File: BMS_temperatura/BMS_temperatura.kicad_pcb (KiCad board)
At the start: 2 copper layers, 100.1 x 100.1 mm, 148 parts, among them J101 Conn_01x08_Male, Q101 MMBT3904, U1 UFRGS_PILL, U101 74HC4051, U103 74HC4051, U105 74HC4051, U112 LM324, U1801 LM324, U1901 LM324, U2001 LM324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

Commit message: layout att 3
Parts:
- TP22: value VCC -> GND
- moved R105 166.8 mm to (98.4, 183.8), turned to 90 degrees
- moved R101 162.1 mm to (81.5, 183.8), turned to 90 degrees
- moved R107 158.7 mm to (116.0, 183.8), turned to 90 degrees
- moved TP27 119.0 mm to (166.7, 163.2)
- moved C106 110.9 mm to (61.3, 153.3)
- moved F301 92.4 mm to (161.5, 101.4), turned to 270 degrees
- moved C103 92.0 mm to (61.3, 151.0)
- moved C101 89.3 mm to (61.3, 148.9)
- moved FB301 84.3 mm to (161.5, 97.0), turned to 270 degrees
- moved TP20 79.9 mm to (110.6, 138.9)
- moved D302 79.8 mm to (83.2, 24.1)
- moved TP18 79.8 mm to (115.5, 135.8)
- moved D301 79.7 mm to (166.5, 100.8), turned to 90 degrees
- moved TP21 74.2 mm to (182.6, 99.9)
- moved TP22 73.4 mm to (163.5, 112.3)
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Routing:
- net GND: track 138.2 -> 290.7 mm, vias 0 -> 2
- net /S2: track 45.3 -> 124.0 mm, vias 3 -> 4
- net /S1: track 45.2 -> 120.3 mm, vias 3 -> 4
- net /S0: track 45.2 -> 116.1 mm
- net +5V: track 276.7 -> 338.9 mm, vias 12 -> 14
- net +12V: track 5.25 -> 62.6 mm
- net /T24: track 1.27 -> 49.3 mm, vias 0 -> 2
- net /T13: track 1.27 -> 39.3 mm, vias 0 -> 2
- net /T5: track 1.27 -> 38.9 mm, vias 0 -> 2
- net /T21: track 1.27 -> 37.9 mm, vias 0 -> 2
- net /T14: track 1.27 -> 33.5 mm, vias 0 -> 2
- net /T23: track 1.27 -> 32.7 mm, vias 0 -> 2
- net /T15: track 1.27 -> 32.2 mm, vias 0 -> 2
- net /T4: track 1.27 -> 32.0 mm, vias 0 -> 2
- net /T12: track 1.27 -> 31.1 mm, vias 0 -> 2
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
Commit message: layout bms temp pronto
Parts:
- removed G104: SYM_LASER_Large, Symbol:WEEE-Logo_8.4x12mm_SilkScreen
- removed TP12: C_ERROR, e-Power:TestPoint_Pad_D1.0mm
- removed TP13: T_ERROR, e-Power:TestPoint_Pad_D1.0mm
- removed TP14: TOUT_3P, e-Power:TestPoint_Pad_D1.0mm
- removed TP22: GND, e-Power:TestPoint_Pad_D1.0mm
- removed TP29: +5V, e-Power:TestPoint_Pad_D1.0mm
- G101: footprint e-Power:Logo_UFRGS_22.0x12.0mm_Mask -> e-Power:Logo_UFRGS_9.2x5.0mm_SilkS
- G102: footprint e-Power:Logo_e-Power_22.8x12.0mm_SilkS -> e-Power:Logo_e-Power_12.4x6.0mm_SilkS
- moved TP9 106.9 mm to (137.8, 145.9)
- moved TP15 106.7 mm to (137.8, 143.6)
- moved D302 105.2 mm to (119.0, 123.1), turned to 180 degrees
- moved TP8 102.0 mm to (137.8, 148.3)
- moved TP10 96.0 mm to (84.4, 119.3)
- moved TP2 90.0 mm to (85.0, 141.3)
- moved TP16 85.4 mm to (96.9, 104.4)
- moved TP1 75.0 mm to (93.1, 138.1)
- moved C106 70.2 mm to (127.2, 177.4), turned to 90 degrees
- moved TP19 67.4 mm to (96.8, 109.0)
- moved G102 67.3 mm to (105.1, 123.0)
- moved G101 64.8 mm to (105.3, 129.8)
- moved TP11 63.0 mm to (96.9, 106.6)
- moved C103 55.4 mm to (109.9, 177.5), turned to 90 degrees
- moved R104 50.9 mm to (94.8, 94.7), turned to 270 degrees
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- renumbered MCP2558 to U110
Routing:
- net GND: track 290.7 -> 598.3 mm, vias 2 -> 13
- net /2.2727V: track 12.3 -> 152.8 mm, vias 0 -> 9
- net /VCC: track 0.00 -> 120.9 mm, vias 0 -> 2
- net /TOUT_1: track 2.16 -> 114.2 mm, vias 0 -> 4
- net /ERROR_TRIG: track 7.49 -> 112.4 mm, vias 0 -> 3
- net +12V: track 62.6 -> 153.1 mm, vias 0 -> 2
- net /TOUT_2P: track 5.82 -> 91.7 mm, vias 0 -> 4
- net /TOUT_3P: track 0.00 -> 84.3 mm, vias 0 -> 2
- net /CAN_H: track 3.53 -> 81.9 mm, vias 0 -> 2
- net +5V: track 338.9 -> 416.3 mm, vias 14 -> 19
- net /CAN_L: track 3.71 -> 76.4 mm, vias 0 -> 3
- net /TOUT_2: track 2.11 -> 73.7 mm, vias 0 -> 2
- net /TOUT_3: track 2.08 -> 72.0 mm, vias 0 -> 5
- net /TOUT_1P: track 3.97 -> 71.2 mm, vias 0 -> 1
- net /RX: track 11.3 -> 66.7 mm, vias 0 -> 2
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
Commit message: layout final bms temp
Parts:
- added G104: SYM_LASER_Large, Symbol:WEEE-Logo_8.4x12mm_SilkScreen, F.Cu at (137.5, 184.6)
- added J1: TEMP_IDC_26_CONN, Connector_IDC:IDC-Header_2x13_P2.54mm_Horizontal, F.Cu at (106.3, 179.5)
- added TP22: GNG, e-Power:TestPoint_Pad_D1.0mm, F.Cu at (99.1, 123.1)
- added TP29: GND, e-Power:TestPoint_Pad_D1.0mm, F.Cu at (145.2, 168.9)
- TP10: value TOUT_3P -> TOUT_1P
- TP11: value VCC -> ~ERROR
- TP2: value TOUT_3P -> TOUT_2P
- moved U2001 48.5 mm to (78.4, 145.3)
- moved C2001 48.5 mm to (78.4, 139.5)
- moved R2002 48.5 mm to (83.7, 147.6)
- moved R2004 48.5 mm to (83.7, 143.0)
- moved R2001 48.5 mm to (73.1, 142.9)
- moved R2003 48.5 mm to (73.1, 147.6)
- moved R1802 43.1 mm to (83.9, 160.7)
- moved R1804 43.1 mm to (83.9, 156.0)
- moved C1801 43.1 mm to (78.5, 152.3)
- moved R1801 43.1 mm to (73.0, 155.7)
- moved R1803 43.1 mm to (73.0, 160.7)
- moved U1801 43.1 mm to (78.4, 158.2)
- moved C103 39.7 mm to (119.6, 138.9), turned to 0 degrees
- moved R105 37.6 mm to (111.5, 148.6)
- moved U103 37.6 mm to (117.3, 145.7)
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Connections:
- U1 pad 40: Net-(U1-Pad40) -> +12V
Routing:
- net /T3: track 8.37 -> 134.3 mm, vias 0 -> 2
- net /T2: track 13.1 -> 128.3 mm, vias 0 -> 2
- net /T4: track 32.0 -> 144.0 mm
- net +5V: track 416.3 -> 527.2 mm, vias 19 -> 22
- net /T1: track 29.2 -> 138.0 mm
- net /T12: track 30.1 -> 126.6 mm
- net /T10: track 12.7 -> 107.1 mm, vias 0 -> 2
- net /T9: track 30.2 -> 119.4 mm
- net /T11: track 8.79 -> 97.9 mm, vias 0 -> 2
- net /TOUT_1: track 114.2 -> 183.2 mm
- net /TOUT_3: track 72.0 -> 138.8 mm, vias 5 -> 2
- net /Temperature Sensors/TS_16: track 3.74 -> 47.9 mm
- net /Temperature Sensors/TS_13: track 3.61 -> 46.8 mm, vias 0 -> 1
- net /Temperature Sensors/TS_1: track 3.66 -> 46.7 mm
- net /Temperature Sensors/TS_4: track 3.76 -> 46.8 mm
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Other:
- board size 100.1 x 100.1 mm -> 100.1 x 115.9 mm

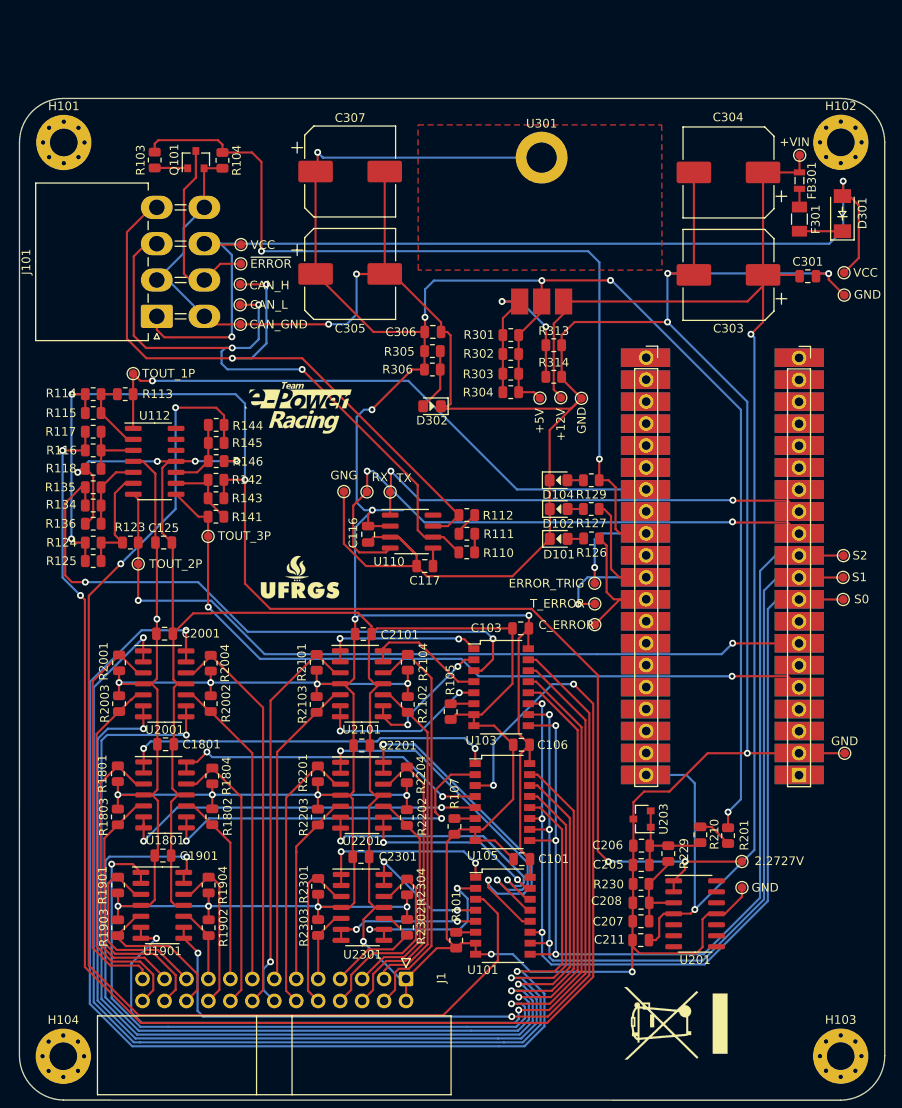
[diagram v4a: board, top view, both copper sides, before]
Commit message: Placa BMS-temperatura
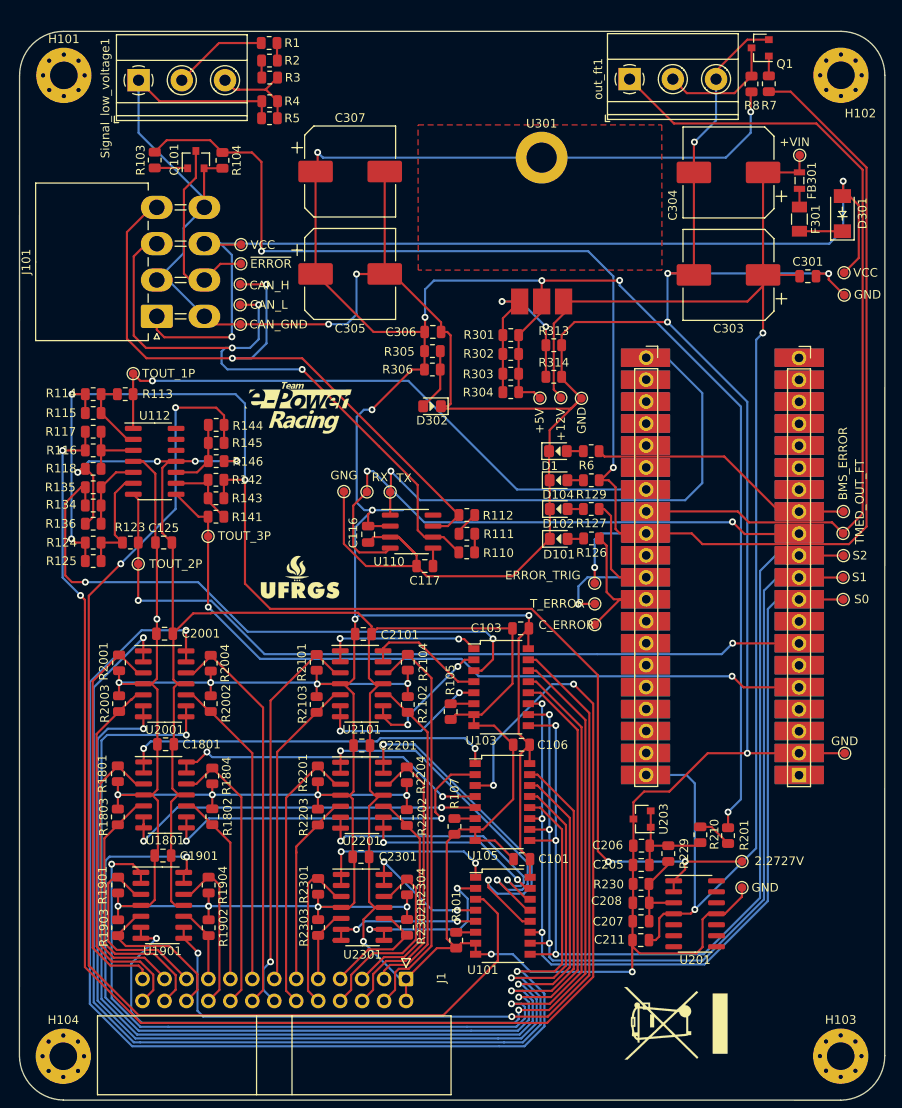
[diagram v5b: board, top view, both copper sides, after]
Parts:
- added D1: LED, e-Power:LED_0805_1.15x1.40mm_HandSolder, F.Cu at (123.9, 118.4)
- added Q1: MMBT3904, Package_TO_SOT_SMD:SOT-23, F.Cu at (147.3, 71.8)
- added R1: 10K, Resistor_SMD:R_0805_2012Metric, F.Cu at (90.5, 71.2)
- added R2: 1K, Resistor_SMD:R_0805_2012Metric, F.Cu at (90.5, 73.3)
- added R3: 1K, Resistor_SMD:R_0805_2012Metric, F.Cu at (90.6, 75.2)
- added R4: 10K, Resistor_SMD:R_0805_2012Metric, F.Cu at (90.6, 78.0)
- added R5: 10K, Resistor_SMD:R_0805_2012Metric, F.Cu at (90.5, 79.9)
- added R6: 1K, Resistor_SMD:R_0805_2012Metric, F.Cu at (127.7, 118.4)
- added R7: 1K, Resistor_SMD:R_0805_2012Metric, F.Cu at (148.3, 75.9)
- added R8: 1K, Resistor_SMD:R_0805_2012Metric, F.Cu at (146.3, 76.0)
- added Signal_low_voltage1: Screw_Terminal_01x03, e-Power:TerminalBlock_Phoenix_MKDS-1,5-3_1x03_P5.00mm_Horizontal, F.Cu at (75.4, 75.5)
- added TP12: TMED_OUT_FT, e-Power:TestPoint_Pad_D1.0mm, F.Cu at (156.9, 127.9)
- added TP13: BMS_ERROR, e-Power:TestPoint_Pad_D1.0mm, F.Cu at (156.9, 125.4)
- added out_ft1: Screw_Terminal_01x03, e-Power:TerminalBlock_Phoenix_MKDS-1,5-3_1x03_P5.00mm_Horizontal, F.Cu at (132.2, 75.4)
- moved H101 7.76 mm to (66.7, 75.0)
- moved H102 7.76 mm to (156.6, 75.0)
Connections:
- U1 pad 13: /TX -> /BMS_ERROR
- U1 pad 21: Net-(U1-Pad21) -> /TX
- U1 pad 28: Net-(U1-Pad28) -> /TMED_OUT_FT
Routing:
- net /TMED_OUT_FT: track 0.00 -> 98.1 mm
- net /ERROR_TRIG: track 112.4 -> 196.0 mm
- net GND: track 618.3 -> 676.1 mm, vias 13 -> 14
- net /BMS_ERROR: track 0.00 -> 31.0 mm
- net +5V: track 527.2 -> 558.0 mm, vias 22 -> 23
- net Net-(Q1-Pad3): track 0.00 -> 14.2 mm
- net Output: track 0.00 -> 11.2 mm
- net Net-(R1-Pad2): track 0.00 -> 11.0 mm
- net /TX: track 54.3 -> 62.0 mm, vias 2 -> 1
- net Net-(Q1-Pad1): track 0.00 -> 2.29 mm
- net Net-(R1-Pad1): track 0.00 -> 2.05 mm
- net Net-(R2-Pad1): track 0.00 -> 1.98 mm
- net Net-(D1-Pad2): track 0.00 -> 1.91 mm
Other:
- board size 100.1 x 115.9 mm -> 100.1 x 123.6 mm
